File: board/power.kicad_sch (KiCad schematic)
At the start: 0 parts

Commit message: Update schematic
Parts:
- added C201: 330u, symbol Device:C_Polarized_Small
- added C202, C203, C210, C211: 10u, symbol Device:C_Small
- added C204, C206: 10n, symbol Device:C_Small
- added C205: 1n, symbol Device:C_Small
- added C207: 39p, symbol Device:C_Small
- added C208: 4n7, symbol Device:C_Small
- added C209, C212: 100n, symbol Device:C_Small
- added C213, C214: 22u, symbol Device:C_Polarized_Small
- added D201: D_TVS, symbol Device:D_TVS
- added D202: 5V6, symbol Device:D_Zener_Small
- added D203: SS34, symbol Device:D_Schottky_Small
- added D204: Power, symbol Device:LED_Small
- added F201: BSMD0805-035, symbol Device:Polyfuse_Small
- added L201: 22u, symbol Device:L_Iron_Small
- added L202: 100R, symbol Device:L_Iron_Small
- added Q201: AO3401A, Package_TO_SOT_SMD:SOT-23, symbol ProjectLibrary:AO3401A
- added R201: 20k, symbol Device:R_Small
- added R202, R204, R205, R207: 10k, symbol Device:R_Small
- added R203: 100k, symbol Device:R_Small
- added R206: 50k, symbol Device:R_Small
- added R208: 750R, symbol Device:R_Small
- added R209, R210: 1k, symbol Device:R_Small
- added U201: TPS54331, Package_SO:SOIC-8_3.9x4.9mm_P1.27mm, symbol ProjectLibrary:TPS54331
- added U202: AMS1117-3.3, Package_TO_SOT_SMD:SOT-223-3_TabPin2, symbol Regulator_Linear:AMS1117-3.3
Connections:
- new net: R202.1, R204.2, R205.1
- new net: C208.2, R206.1
- new net: R208.2, R209.1
- new net: D202.2 (A), Q201.1 (G), R201.1
- new net +3V3: D204.2 (A), F201.1
- new net +5V: C210.1, C211.1, C212.1, L201.2, L202.1, R207.1
- new net BUCK_BOOT: C209.1, U201.1 (BOOT)
- new net BUCK_CP: C207.1, C208.1, U201.6 (COMP)
- new net BUCK_EN: R203.2, R204.1, U201.3 (EN)
- new net BUCK_PH: C209.2, D203.1 (K), L201.1, U201.8 (PH)
- new net BUCK_SS: C206.1, U201.4 (SS)
- new net BUCK_VSENSE: R207.2, R208.1, U201.5 (VSENSE)
- new net EXT_VCC: D201.2 (A2), Q201.3 (D)
- new net GND: C201.2, C202.2, C203.2, C204.2, C205.2, C206.2, C207.2, C210.2, C211.2, C212.2, C213.2, C214.2, D201.1 (A1), D203.2 (A), R201.2, R202.2, R205.2, R206.2, R209.2, R210.1, U201.7 (GND), U202.1 (GND)
- new net LDO_VI: C213.1, L202.2, U202.3 (VI)
- new net LDO_VO: C214.1, F201.2, U202.2 (VO)
- new net POWER_LED_K: D204.1 (K), R210.2
- new net VCC: C201.1, C202.1, C203.1, C204.1, C205.1, D202.1 (K), Q201.2 (S), R203.1, U201.2 (VIN)
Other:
- note added: "+3V3 Regulator"
- note added: "+5V Regulator"
- note added: "ESD Protection and reverse polarity protection."
- note added: "Input Caps Min 20V 1A Low ESR"
- note added: "Iout(max)=1A"
- note added: "Output Caps Min 6V 1.5A Low ESR"
- note added: "Power"
- note added: "Power Indicator"
- note added: "TODO FIX (now out is 5V4)"
- note added: "Use tantalum caps with 0.2Ω < ESR < 22Ω."
- note added: "V(EN,HI)=1.25V UVLO @ VIN= 9.0V"
- note added: "VCC Supply"
- note added: "VCC(min) = 9.0V VCC(max) = 15.0V"
- note added: "Vsense=0.8V"
- company: (none) -> BlueDot, Vincenzo Fortunato
- title: (none) -> BD845-PWB

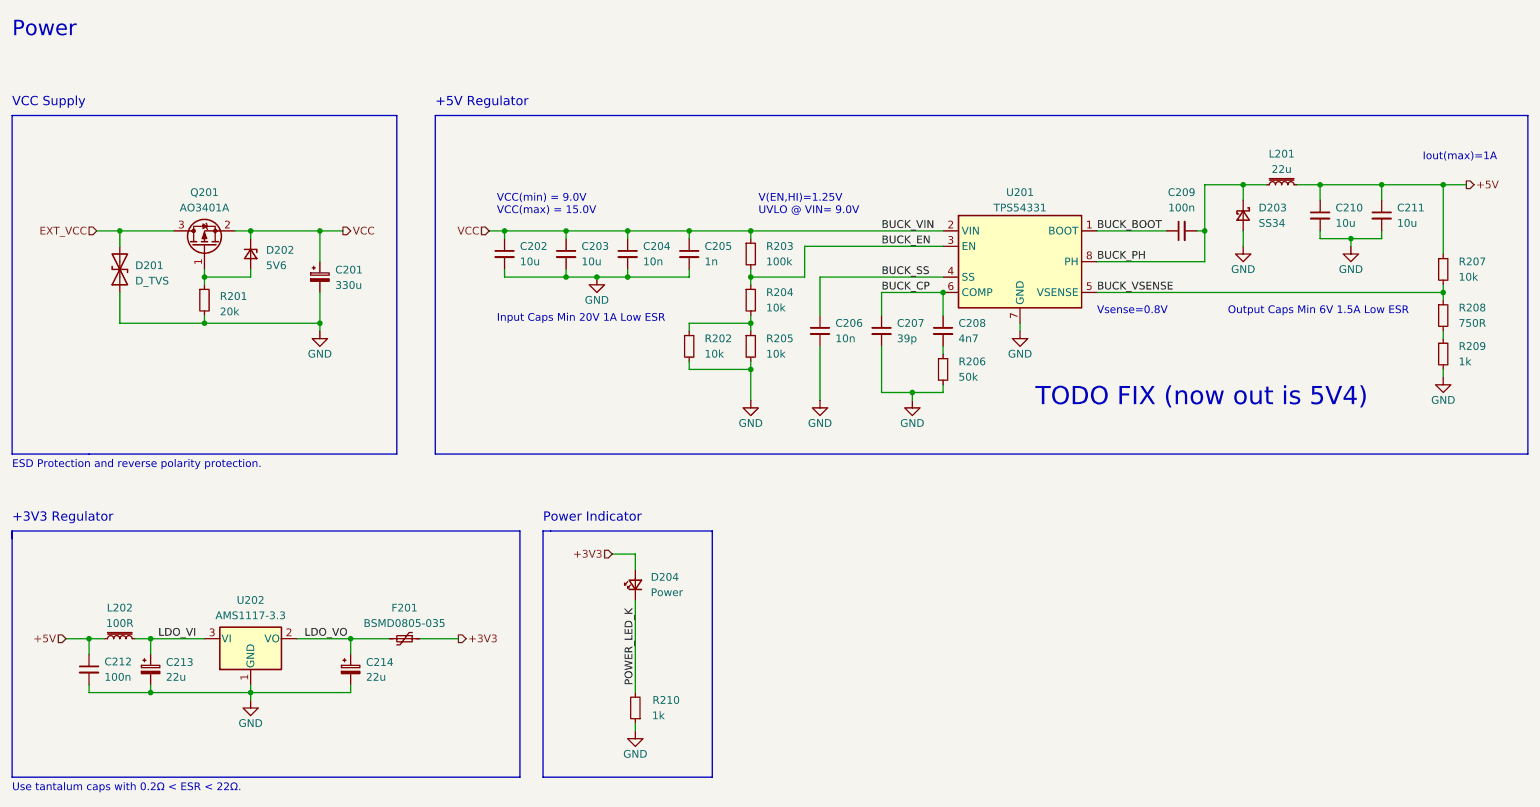
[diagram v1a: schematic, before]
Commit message: Schematic done
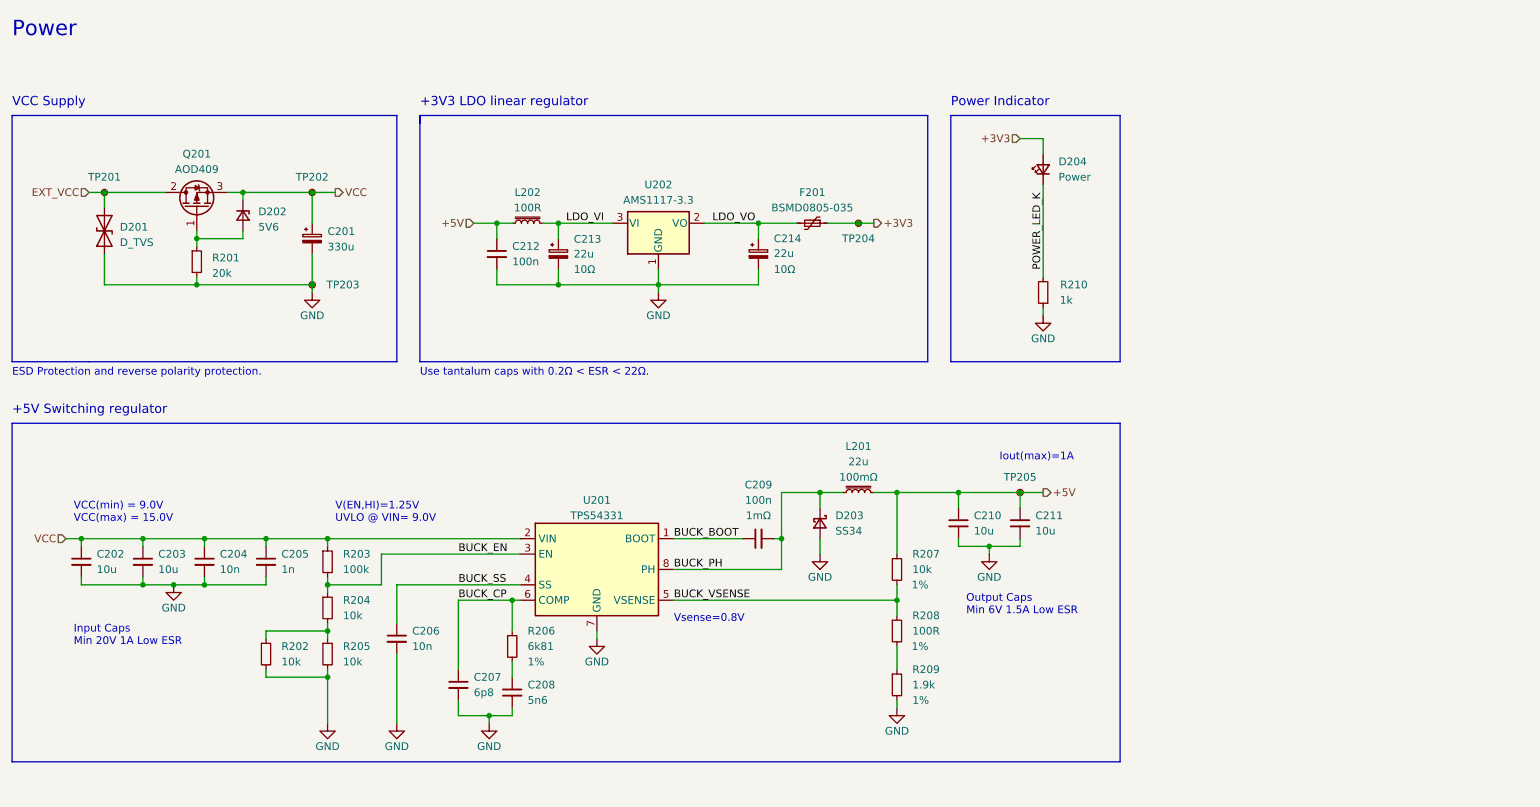
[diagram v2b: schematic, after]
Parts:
- removed Q201: AO3401A, Package_TO_SOT_SMD:SOT-23, symbol ProjectLibrary:AO3401A
- added Q201: AOD409, Package_TO_SOT_SMD:TO-252-3_TabPin2, symbol ProjectLibrary:AOD409
- added TP201, TP202, TP203, TP204, TP205: TestPoint_Small, TestPoint:TestPoint_Pad_D1.0mm, symbol Connector:TestPoint_Small
- C201: footprint (none) -> Capacitor_THT:CP_Radial_D8.0mm_P3.50mm
- C202, C203, C204, C205, C206, C210, C211, C212: footprint (none) -> Capacitor_SMD:C_0603_1608Metric
- C207: value 39p -> 6p8; footprint (none) -> Capacitor_SMD:C_0603_1608Metric
- C208: value 4n7 -> 5n6; footprint (none) -> Capacitor_SMD:C_0603_1608Metric
- C209: footprint (none) -> Capacitor_SMD:C_0603_1608Metric; ESR (none) -> 1mΩ
- C213, C214: footprint (none) -> Capacitor_Tantalum_SMD:CP_EIA-3528-15_AVX-H; ESR (none) -> 10Ω
- D201, D203: footprint (none) -> Diode_SMD:D_SMA
- D202: footprint (none) -> Diode_SMD:D_MiniMELF
- D204: footprint (none) -> LED_SMD:LED_0805_2012Metric
- F201: footprint (none) -> Fuse:Fuse_0805_2012Metric
- L201: footprint (none) -> Inductor_SMD:L_Taiyo-Yuden_NR-50xx; ESR (none) -> 100mΩ
- L202: footprint (none) -> Resistor_SMD:R_0805_2012Metric
- R201, R202, R203, R204, R205, R210: footprint (none) -> Resistor_SMD:R_0603_1608Metric
- R206: value 50k -> 6k81; footprint (none) -> Resistor_SMD:R_0603_1608Metric; Accuracy (none) -> 1%
- R207: footprint (none) -> Resistor_SMD:R_0603_1608Metric; Accuracy (none) -> 1%
- R208: value 750R -> 100R; footprint (none) -> Resistor_SMD:R_0603_1608Metric; Accuracy (none) -> 1%
- R209: value 1k -> 1.9k; footprint (none) -> Resistor_SMD:R_0603_1608Metric; Accuracy (none) -> 1%
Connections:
- net +3V3: now also TP204.1
- net +5V: now also TP205.1
- net BUCK_CP: now also R206.1; no longer C208.1
- net EXT_VCC: now also Q201.2 (D), TP201.1
- net GND: now also C208.2, TP203.1; no longer R206.2
- net VCC: now also Q201.3 (S), TP202.1
- net at D202.2 (A), R201.1: now also Q201.1 (G)
- new net: C208.1, R206.2
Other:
- note added: "+3V3 LDO linear regulator"
- note added: "+5V Switching regulator"
- note removed: "+3V3 Regulator"
- note removed: "+5V Regulator"
- note removed: "TODO FIX (now out is 5V4)"
- moved on the sheet: C201, C202, C203, C204, C205, C206, C207, C208, C209, C212, C213, C214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

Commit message: Update PCB
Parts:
- removed TP201: TestPoint_Small, TestPoint:TestPoint_Pad_D1.0mm, symbol Connector:TestPoint_Small
- renumbered TP202 to TP201, TP203 to TP202, TP204 to TP203, TP205 to TP204
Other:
- moved on the sheet: C207
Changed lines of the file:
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@@
     (stroke (width 0) (type default))
   )
-  (wire (pts (xy 96.52 137.16) (xy 96.52 139.7))
+  (wire (pts (xy 96.52 138.43) (xy 96.52 139.7))
     (stroke (width 0) (type default))
   )
@@
     (stroke (width 0) (type default))
   )
-  (wire (pts (xy 96.52 120.65) (xy 96.52 132.08))
+  (wire (pts (xy 96.52 120.65) (xy 96.52 133.35))
     (stroke (width 0) (type default))
   )
@@
     )
   )
-  (symbol (lib_id "Connector:TestPoint_Small") (at 38.1 53.34 0) (unit 1)
-    (in_bom yes) (on_board yes) (dnp no)
-    (property "Reference" "TP201" (at 38.1 50.8 0)
-      (effects (font (size 1.27 1.27)))
-    )
-    (property "Value" "TestPoint_Small" (at 39.37 55.245 0)
-      (effects (font (size 1.27 1.27)) (justify left) hide)
-    )
-    (property "Footprint" "TestPoint:TestPoint_Pad_D1.0mm" (at 43.18 53.34 0)
-      (effects (font (size 1.27 1.27)) hide)
-    )
-    (property "Datasheet" "~" (at 43.18 53.34 0)
-      (effects (font (size 1.27 1.27)) hide)
-    )
-    (pin "1")
-    (instances
-      (project "bd845-pwb"
-        (path "/c0443f53-6229-4858-b0f1-180b8ed8e6c2/b87f26e1-1b9c-4de9-9564-59105313047d"
-          (reference "TP201") (unit 1) (value "TestPoint_Small") (footprint "TestPoint:TestPoint_Pad_D1.0mm")
-        )
-      )
-    )
-  )
   (symbol (lib_id "Connector:TestPoint_Small") (at 162.56 58.42 0) (unit 1)
     (in_bom yes) (on_board yes) (dnp no)
-    (property "Reference" "TP204" (at 162.56 60.96 0)
+    (property "Reference" "TP203" (at 162.56 60.96 0)
       (effects (font (size 1.27 1.27)))
     )
@@
       (project "bd845-pwb"
         (path "/c0443f53-6229-4858-b0f1-180b8ed8e6c2/b87f26e1-1b9c-4de9-9564-59105313047d"
-          (reference "TP204") (unit 1) (value "TestPoint_Small") (footprint "TestPoint:TestPoint_Pad_D1.0mm")
+          (reference "TP203") (unit 1) (value "TestPoint_Small") (footprint "TestPoint:TestPoint_Pad_D1.0mm")
         )
       )
@@
   (symbol (lib_id "Connector:TestPoint_Small") (at 72.39 53.34 0) (unit 1)
     (in_bom yes) (on_board yes) (dnp no)
-    (property "Reference" "TP202" (at 72.39 50.8 0)
+    (property "Reference" "TP201" (at 72.39 50.8 0)
       (effects (font (size 1.27 1.27)))
     )
@@
       (project "bd845-pwb"
         (path "/c0443f53-6229-4858-b0f1-180b8ed8e6c2/b87f26e1-1b9c-4de9-9564-59105313047d"
-          (reference "TP202") (unit 1) (value "TestPoint_Small") (footprint "TestPoint:TestPoint_Pad_D1.0mm")
+          (reference "TP201") (unit 1) (value "TestPoint_Small") (footprint "TestPoint:TestPoint_Pad_D1.0mm")
         )
       )
@@
   (symbol (lib_id "Connector:TestPoint_Small") (at 189.23 102.87 0) (unit 1)
     (in_bom yes) (on_board yes) (dnp no)
-    (property "Reference" "TP205" (at 189.23 100.33 0)
+    (property "Reference" "TP204" (at 189.23 100.33 0)
       (effects (font (size 1.27 1.27)))
     )
@@
       (project "bd845-pwb"
         (path "/c0443f53-6229-4858-b0f1-180b8ed8e6c2/b87f26e1-1b9c-4de9-9564-59105313047d"
-          (reference "TP205") (unit 1) (value "TestPoint_Small") (footprint "TestPoint:TestPoint_Pad_D1.0mm")
+          (reference "TP204") (unit 1) (value "TestPoint_Small") (footprint "TestPoint:TestPoint_Pad_D1.0mm")
         )
       )
@@
     )
   )
-  (symbol (lib_id "Device:C_Small") (at 96.52 134.62 0) (unit 1)
-    (in_bom yes) (on_board yes) (dnp no)
-    (property "Reference" "C207" (at 99.06 133.35 0)
-      (effects (font (size 1.27 1.27)) (justify left))
-    )
-    (property "Value" "6p8" (at 99.06 135.89 0)
-      (effects (font (size 1.27 1.27)) (justify left))
-    )
-    (property "Footprint" "Capacitor_SMD:C_0603_1608Metric" (at 96.52 134.62 0)
-      (effects (font (size 1.27 1.27)) hide)
-    )
-    (property "Datasheet" "~" (at 96.52 134.62 0)
+  (symbol (lib_id "Device:C_Small") (at 96.52 135.89 0) (unit 1)
+    (in_bom yes) (on_board yes) (dnp no)
+    (property "Reference" "C207" (at 99.06 134.62 0)
+      (effects (font (size 1.27 1.27)) (justify left))
+    )
+    (property "Value" "6p8" (at 99.06 137.16 0)
+      (effects (font (size 1.27 1.27)) (justify left))
+    )
+    (property "Footprint" "Capacitor_SMD:C_0603_1608Metric" (at 96.52 135.89 0)
+      (effects (font (size 1.27 1.27)) hide)
+    )
+    (property "Datasheet" "~" (at 96.52 135.89 0)
       (effects (font (size 1.27 1.27)) hide)
     )
@@
   (symbol (lib_id "Connector:TestPoint_Small") (at 72.39 68.58 0) (unit 1)
     (in_bom yes) (on_board yes) (dnp no)
-    (property "Reference" "TP203" (at 77.47 68.58 0)
+    (property "Reference" "TP202" (at 77.47 68.58 0)
       (effects (font (size 1.27 1.27)))
     )
@@
       (project "bd845-pwb"
         (path "/c0443f53-6229-4858-b0f1-180b8ed8e6c2/b87f26e1-1b9c-4de9-9564-59105313047d"
-          (reference "TP203") (unit 1) (value "TestPoint_Small") (footprint "TestPoint:TestPoint_Pad_D1.0mm")
-        )
-      )
+          (reference "TP202") (unit 1) (value "TestPoint_Small") (footprint "TestPoint:TestPoint_Pad_D1.0mm")
+        )
+      )

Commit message: Update PCB
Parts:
- R201: value 20k -> 10k
- R208: value 100R -> 150R
- R209: value 1.9k -> 1k8
- R210: value 1k -> 330R
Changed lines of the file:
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@@
       (effects (font (size 1.27 1.27)) (justify left))
     )
-    (property "Value" "1.9k" (at 171.45 134.62 0)
+    (property "Value" "1k8" (at 171.45 134.62 0)
       (effects (font (size 1.27 1.27)) (justify left))
     )
@@
       (project "bd845-pwb"
         (path "/c0443f53-6229-4858-b0f1-180b8ed8e6c2/b87f26e1-1b9c-4de9-9564-59105313047d"
-          (reference "R209") (unit 1) (value "1.9k") (footprint "Resistor_SMD:R_0603_1608Metric")
+          (reference "R209") (unit 1) (value "1k8") (footprint "Resistor_SMD:R_0603_1608Metric")
         )
       )
@@
       (effects (font (size 1.27 1.27)) (justify left))
     )
-    (property "Value" "20k" (at 55.88 66.675 0)
+    (property "Value" "10k" (at 55.88 66.675 0)
       (effects (font (size 1.27 1.27)) (justify left))
     )
@@
       (project "bd845-pwb"
         (path "/c0443f53-6229-4858-b0f1-180b8ed8e6c2/b87f26e1-1b9c-4de9-9564-59105313047d"
-          (reference "R201") (unit 1) (value "20k") (footprint "Resistor_SMD:R_0603_1608Metric")
+          (reference "R201") (unit 1) (value "10k") (footprint "Resistor_SMD:R_0603_1608Metric")
         )
       )
@@
       (effects (font (size 1.27 1.27)) (justify left))
     )
-    (property "Value" "100R" (at 171.45 125.73 0)
+    (property "Value" "150R" (at 171.45 125.73 0)
       (effects (font (size 1.27 1.27)) (justify left))
     )
@@
       (project "bd845-pwb"
         (path "/c0443f53-6229-4858-b0f1-180b8ed8e6c2/b87f26e1-1b9c-4de9-9564-59105313047d"
-          (reference "R208") (unit 1) (value "100R") (footprint "Resistor_SMD:R_0603_1608Metric")
+          (reference "R208") (unit 1) (value "150R") (footprint "Resistor_SMD:R_0603_1608Metric")
         )
       )
@@
   (symbol (lib_id "Device:R_Small") (at 193.04 69.85 180) (unit 1)
     (in_bom yes) (on_board yes) (dnp no)
-    (property "Reference" "R210" (at 198.12 68.58 0)
-      (effects (font (size 1.27 1.27)))
-    )
-    (property "Value" "1k" (at 196.85 71.12 0)
-      (effects (font (size 1.27 1.27)))
+    (property "Reference" "R210" (at 195.58 68.58 0)
+      (effects (font (size 1.27 1.27)) (justify right))
+    )
+    (property "Value" "330R" (at 195.58 71.12 0)
+      (effects (font (size 1.27 1.27)) (justify right))
     )
     (property "Footprint" "Resistor_SMD:R_0603_1608Metric" (at 193.04 69.85 0)
@@
       (project "bd845-pwb"
         (path "/c0443f53-6229-4858-b0f1-180b8ed8e6c2/b87f26e1-1b9c-4de9-9564-59105313047d"
-          (reference "R210") (unit 1) (value "1k") (footprint "Resistor_SMD:R_0603_1608Metric")
-        )
-      )
+          (reference "R210") (unit 1) (value "330R") (footprint "Resistor_SMD:R_0603_1608Metric")
+        )
+      )

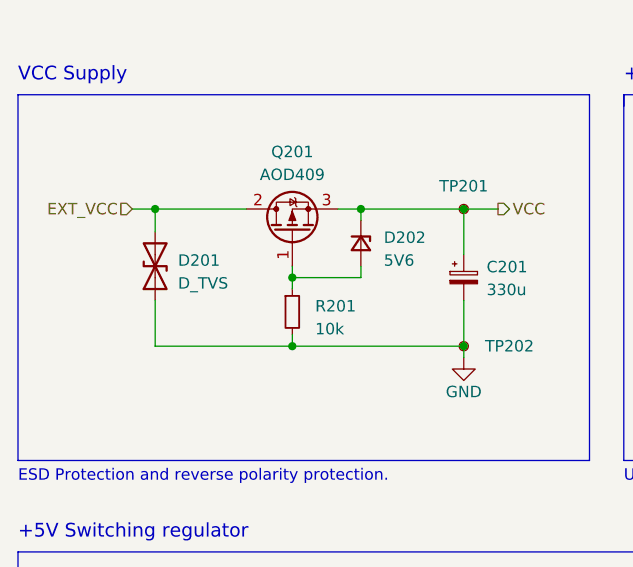
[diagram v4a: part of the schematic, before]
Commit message: Select input TVS diode
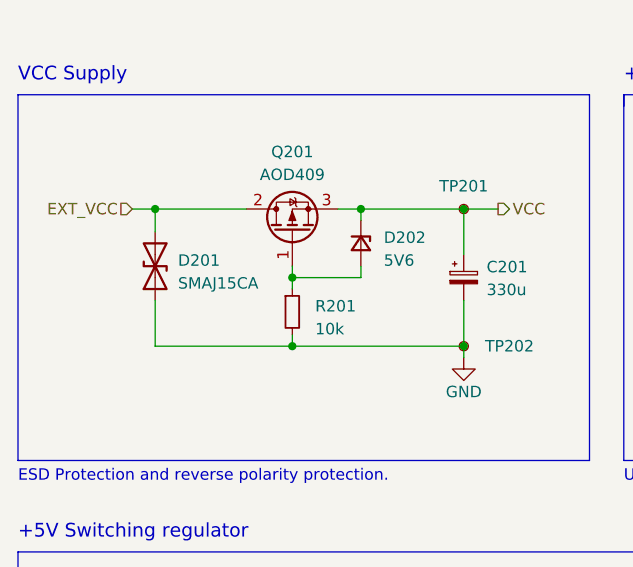
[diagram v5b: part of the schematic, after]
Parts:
- D201: value D_TVS -> SMAJ15CA
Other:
- title: BD845-PWB -> BD845-PWB SCH
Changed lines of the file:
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@@
   (paper "A4")
   (title_block
-    (title "BD845-PWB")
+    (title "BD845-PWB SCH")
     (date "2022-11-27")
-    (rev "1")
+    (rev "1.0.0")
     (company "BlueDot, Vincenzo Fortunato")
   )
@@
       (effects (font (size 1.27 1.27)) (justify right))
     )
-    (property "Value" "D_TVS" (at 40.64 61.595 90)
+    (property "Value" "SMAJ15CA" (at 40.64 61.595 90)
       (effects (font (size 1.27 1.27)) (justify right))
     )
@@
       (project "bd845-pwb"
         (path "/c0443f53-6229-4858-b0f1-180b8ed8e6c2/b87f26e1-1b9c-4de9-9564-59105313047d"
-          (reference "D201") (unit 1) (value "D_TVS") (footprint "Diode_SMD:D_SMA")
+          (reference "D201") (unit 1) (value "SMAJ15CA") (footprint "Diode_SMD:D_SMA")
         )
       )

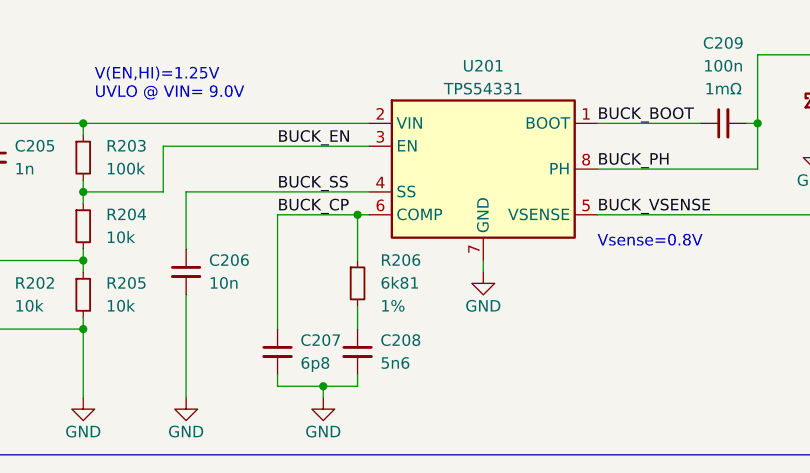
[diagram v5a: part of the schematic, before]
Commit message: Update connectors color
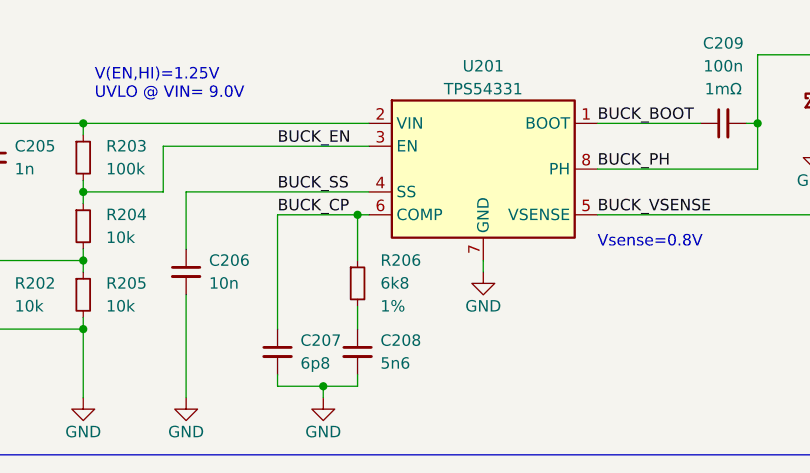
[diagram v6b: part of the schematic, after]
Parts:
- R206: value 6k81 -> 6k8
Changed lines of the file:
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@@
       (effects (font (size 1.27 1.27)) (justify left))
     )
-    (property "Value" "6k81" (at 107.95 128.2637 0)
+    (property "Value" "6k8" (at 107.95 128.2637 0)
       (effects (font (size 1.27 1.27)) (justify left))
     )
@@
       (project "bd845-pwb"
         (path "/c0443f53-6229-4858-b0f1-180b8ed8e6c2/b87f26e1-1b9c-4de9-9564-59105313047d"
-          (reference "R206") (unit 1) (value "6k81") (footprint "Resistor_SMD:R_0603_1608Metric")
+          (reference "R206") (unit 1) (value "6k8") (footprint "Resistor_SMD:R_0603_1608Metric")
         )
       )
